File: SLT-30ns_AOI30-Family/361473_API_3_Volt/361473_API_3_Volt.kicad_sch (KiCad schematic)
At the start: 9 parts, among them T1 ABA, U1 12-Pin_SLx_Can

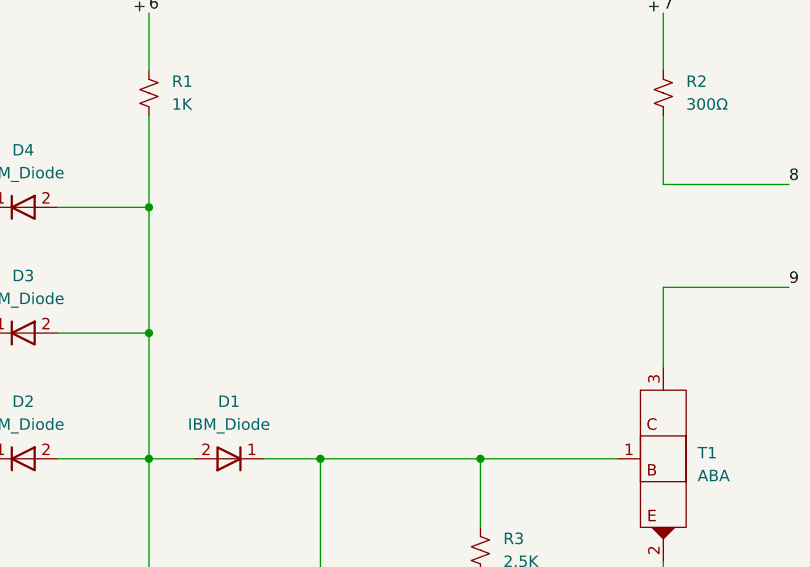
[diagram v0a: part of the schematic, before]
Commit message: Update schematic pdfs
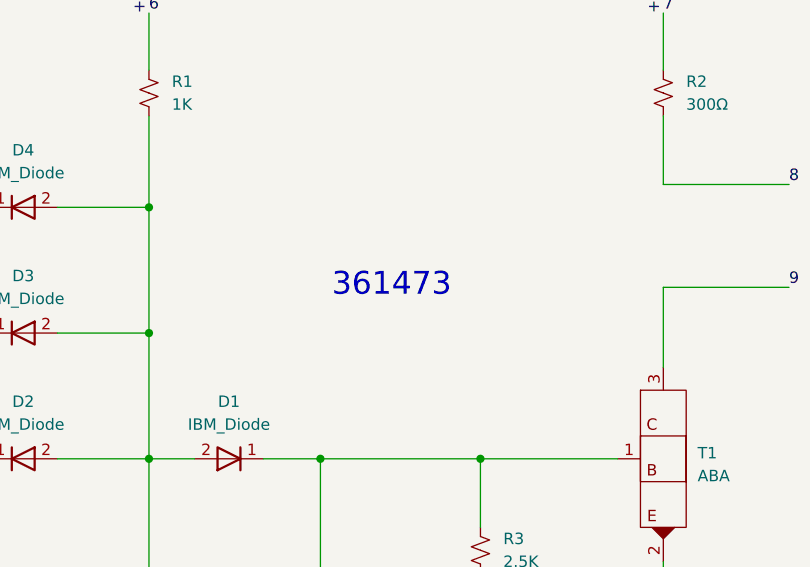
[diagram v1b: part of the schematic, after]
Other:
- note added: "361473"
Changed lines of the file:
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@@
     (stroke (width 0) (type default) (color 0 0 0 0))
+  )
+  (text "361473" (at 119.38 76.2 0)
+    (effects (font (size 2.54 2.54)) (justify left bottom))
   )
   (label "8" (at 170.18 63.5 0)
